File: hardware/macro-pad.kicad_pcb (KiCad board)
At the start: 2 copper layers, 94 x 71 mm, 43 parts, among them J1 USB_C_Receptacle_USB2.0, SW1 PEC12R-4025F-S0024, SW2 MX1A-G1NA, SW3 MX1A-G1NA, SW4 MX1A-G1NA, SW5 MX1A-G1NA, U1 MIC5317-3.3ZD5-TR, U2 RP2040, U3 W25Q128JVSIQ, Y1 ABLS-12.000MHZ-B4-T

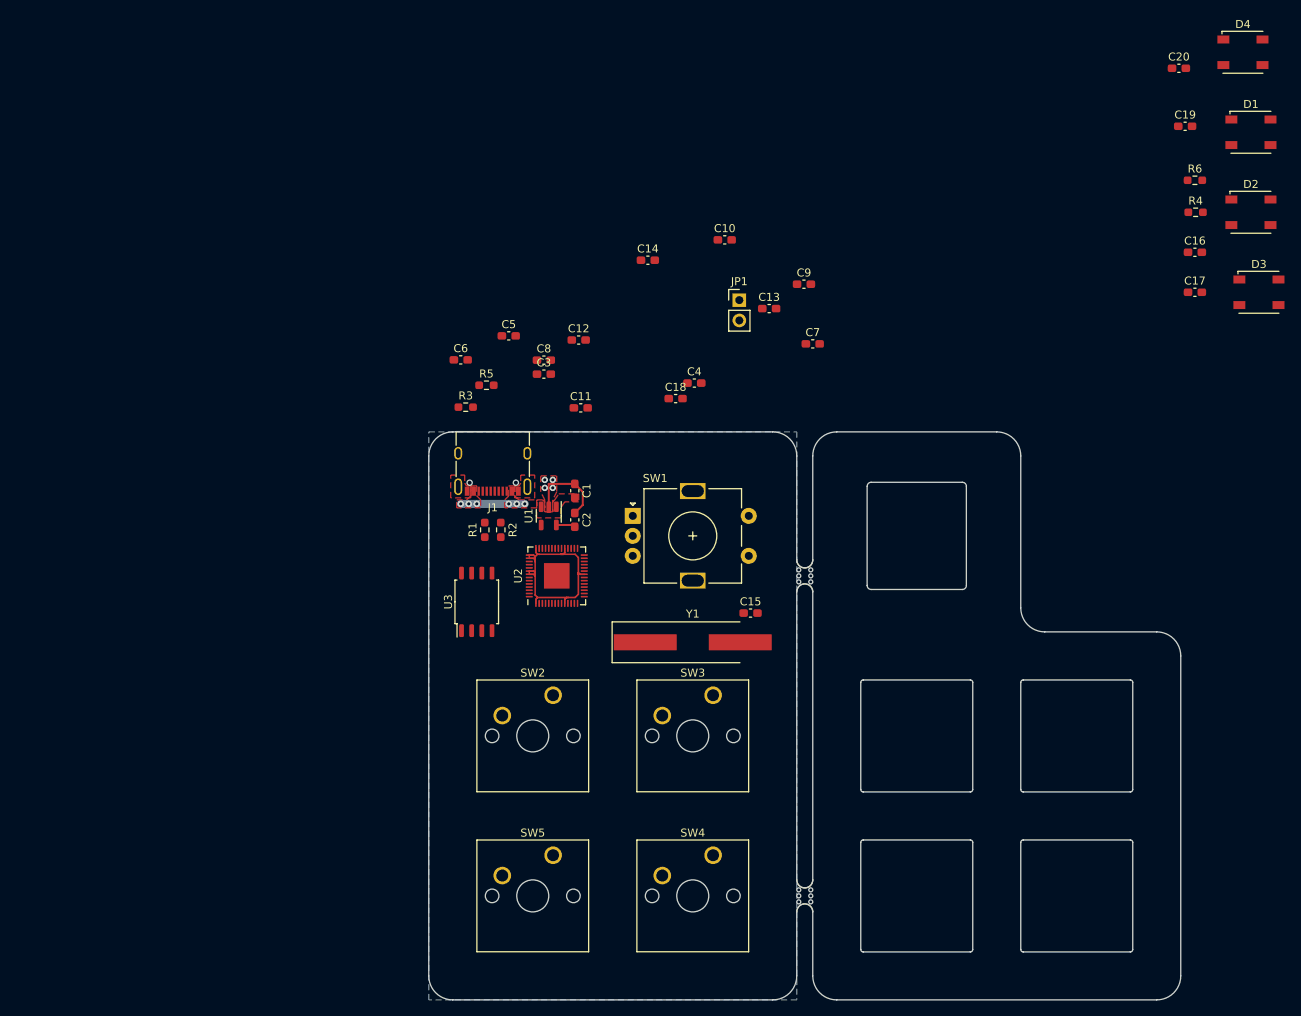
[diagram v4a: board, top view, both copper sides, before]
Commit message: Added LED data and power traces
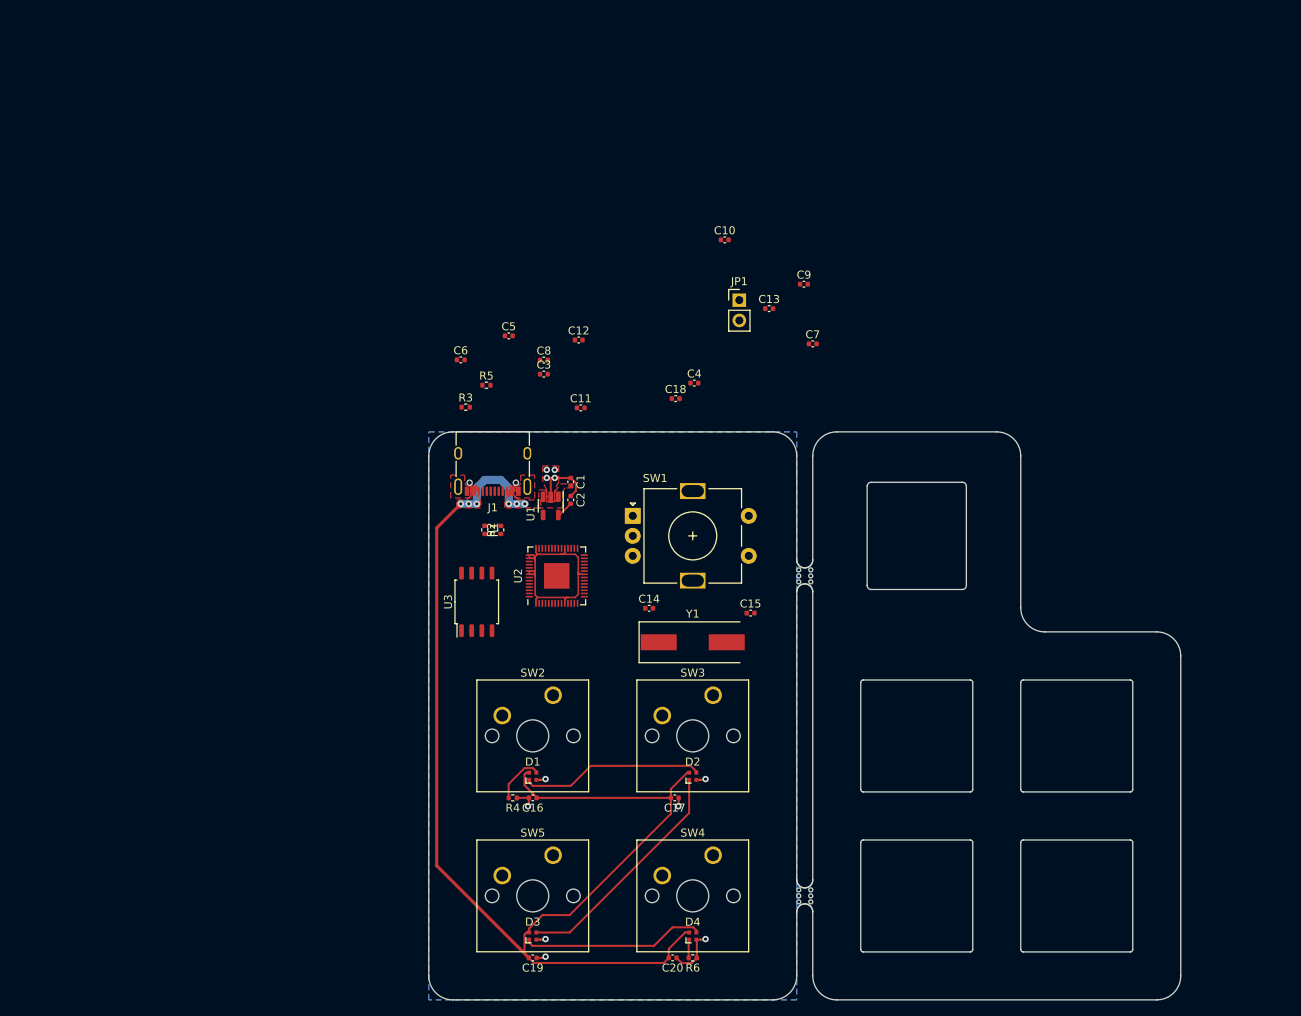
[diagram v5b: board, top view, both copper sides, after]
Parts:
- C1, C10, C11, C12, C13, C14, C15, C16, C17, C18, C19, C2, C20, C3, C4, C5, C6, C7, C8, C9: footprint Capacitor_SMD:C_0603_1608Metric_Pad1.08x0.95mm_HandSolder -> Capacitor_SMD:C_0402_1005Metric
- D1, D2, D3, D4: footprint LED_SMD:LED_Inolux_IN-PI554FCH_PLCC4_5.0x5.0mm_P3.2mm -> LED_SMD:LED_SK6812_EC15_1.5x1.5mm
- R1, R2, R3, R4, R5, R6: footprint Resistor_SMD:R_0603_1608Metric_Pad0.98x0.95mm_HandSolder -> Resistor_SMD:R_0402_1005Metric
- Y1: footprint Crystal:Crystal_SMD_HC49-SD_HandSoldering -> Crystal:Crystal_SMD_HC49-SD
- moved C19 132.1 mm to (110.0, 137.8)
- moved D4 130.1 mm to (130.0, 135.0), turned to 180 degrees
- moved C20 127.9 mm to (127.5, 137.8)
- moved D3 121.3 mm to (110.0, 135.0), turned to 180 degrees
- moved D1 120.6 mm to (110.0, 115.0), turned to 180 degrees
- moved R6 115.7 mm to (130.0, 137.8)
- moved R4 112.4 mm to (107.5, 117.8)
- moved C16 107.2 mm to (110.0, 117.8), turned to 180 degrees
- moved D2 99.2 mm to (130.0, 115.0), turned to 180 degrees
- moved C17 90.7 mm to (127.8, 117.8)
- moved C14 43.5 mm to (124.5, 94.0)
- moved C2 2.55 mm to (114.8, 80.5)
- moved U1 1.27 mm to (112.2, 81.2)
- moved C1 1.22 mm to (114.8, 78.2)
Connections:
- D1 pad 2: Net-(D1-Pad2) -> /D_{LED}
- D2 pad 2: Net-(D2-Pad2) -> Net-(D1-Pad4)
- D2 pad 4: Net-(D1-Pad2) -> Net-(D2-Pad4)
- D3 pad 2: Net-(D3-Pad2) -> Net-(D2-Pad4)
- D3 pad 4: Net-(D2-Pad2) -> Net-(D3-Pad4)
- D4 pad 2: /D_{LED} -> Net-(D3-Pad4)
- D4 pad 4: Net-(D3-Pad2) -> Net-(D4-Pad4)
- R4 pad 1: Net-(D1-Pad4) -> /D_{LED}
- R6 pad 1: /D_{LED} -> Net-(D4-Pad4)
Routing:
- net +5V: track 8.00 -> 153.3 mm
- net Net-(D2-Pad4): track 0.00 -> 29.4 mm
- net Net-(D1-Pad4): track 0.00 -> 22.9 mm
- net Net-(D3-Pad4): track 0.00 -> 22.8 mm
- net GND: track 10.6 -> 22.6 mm, vias 4 -> 11
- net /D_{LED}: track 0.00 -> 6.35 mm
- net Net-(D4-Pad4): track 0.00 -> 2.30 mm

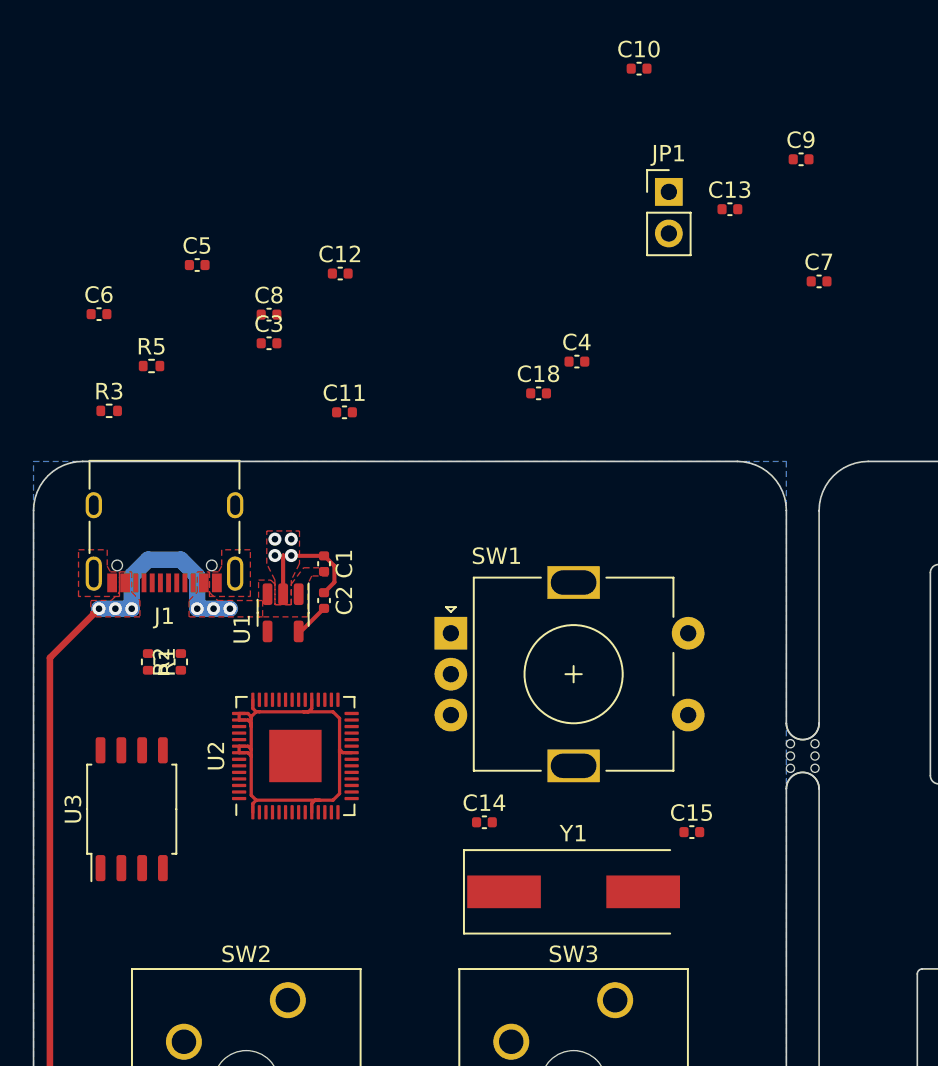
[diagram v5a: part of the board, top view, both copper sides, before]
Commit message: Processor and memory secion finished and wired up
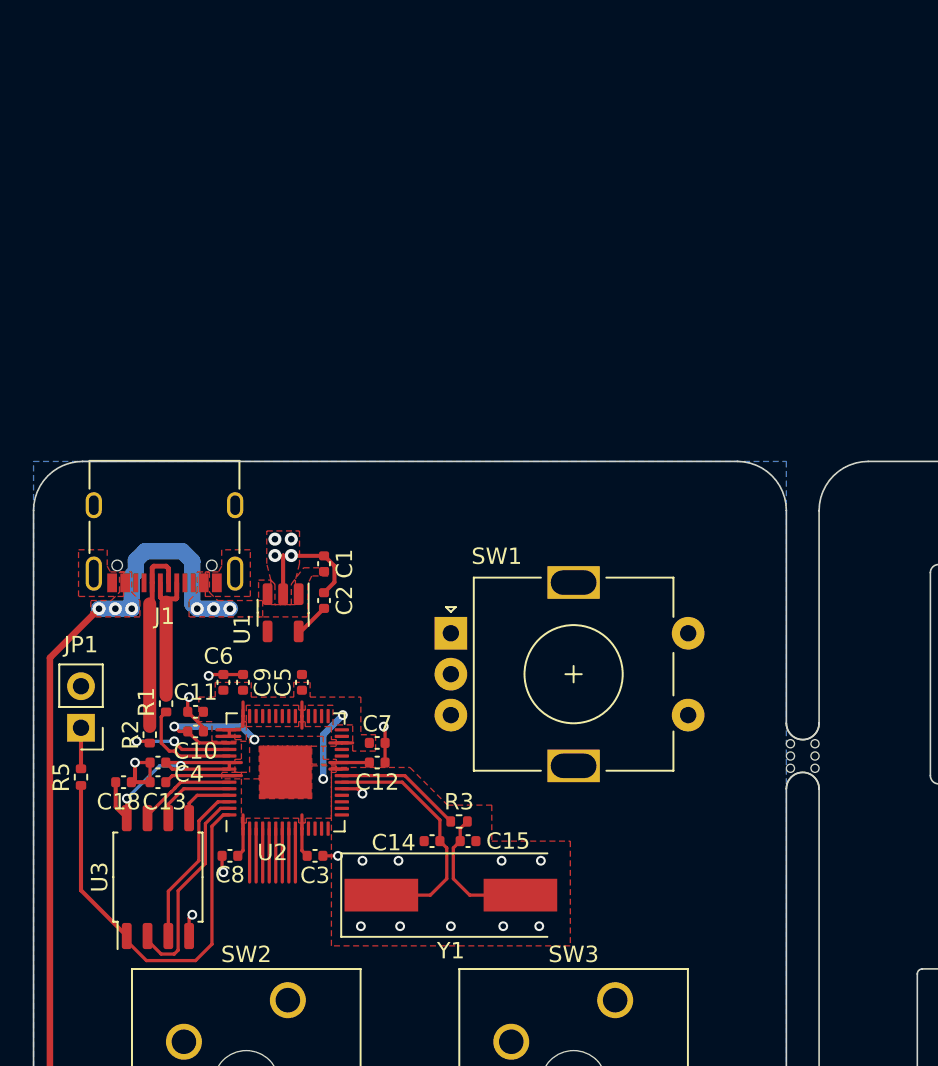
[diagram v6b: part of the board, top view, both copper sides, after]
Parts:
- moved C13 49.5 mm to (104.6, 91.6), turned to 180 degrees
- moved JP1 48.6 mm to (99.9, 88.3), turned to 180 degrees
- moved C10 47.7 mm to (106.9, 87.3), turned to 180 degrees
- moved C9 46.7 mm to (109.8, 85.5), turned to 90 degrees
- moved C7 39.0 mm to (118.0, 89.2)
- moved C4 35.4 mm to (104.6, 90.4), turned to 180 degrees
- moved C18 34.8 mm to (102.5, 91.6)
- moved C8 33.2 mm to (109.0, 96.1), turned to 180 degrees
- moved R3 33.0 mm to (123.0, 94.0), turned to 180 degrees
- moved C3 31.4 mm to (114.2, 96.1)
- moved C12 30.0 mm to (118.0, 90.4)
- moved C5 26.3 mm to (113.4, 85.5), turned to 90 degrees
- moved R5 25.5 mm to (99.9, 91.3), turned to -90 degrees
- moved C6 23.7 mm to (108.6, 85.5), turned to 90 degrees
- moved C11 21.5 mm to (106.9, 88.5)
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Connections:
- net Net-(R1-Pad2) renamed /DP
- net Net-(R2-Pad1) renamed /DN
- U2 pad 26: +3.3V -> +3V3
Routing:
- net /QSPI_{SS}: track 0.00 -> 25.3 mm
- net +1V1: track 0.00 -> 16.2 mm, vias 0 -> 2
- net GND: track 22.6 -> 38.8 mm, vias 11 -> 28
- net /X_{IN}: track 0.00 -> 15.2 mm
- net /QSPI_{SD}1: track 0.00 -> 12.9 mm
- net /D_{USB}-: track 0.00 -> 11.7 mm
- net /QSPI_{SD}2: track 0.00 -> 10.2 mm
- net /D_{USB}+: track 0.00 -> 8.56 mm
- net Net-(C15-Pad1): track 0.00 -> 8.37 mm
- net /X_{OUT}: track 0.00 -> 7.81 mm
- net /DN: track 0.00 -> 6.73 mm, vias 0 -> 2
- net /DP: track 0.00 -> 6.51 mm
- net /QSPI_{SD}3: track 0.00 -> 6.01 mm
- net +3V3: track 32.3 -> 37.3 mm, vias 0 -> 4
- net /QSPI_{SCLK}: track 0.00 -> 4.98 mm
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- added copper zone on F.Cu, net +1V1
- added copper zone on F.Cu, net +3V3
